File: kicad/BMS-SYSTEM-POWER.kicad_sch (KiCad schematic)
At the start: 80 parts, among them J1 BATTERY, J2 USB C, Q1 AO4435, Q11 2N3904, Q17 2N3904, Q2 AO4468, Q3 PNP-SOT23, Q4 WST4041, Q5 AO3401, U1 SGM6132YPS8G/TR, U2 CN3303, U4 SY8089A, U5 SY8089A, U6 INA180A2IDBVR

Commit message: Battery charging
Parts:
- removed C4, C7: 22uF, oomwoo_altium:C1206, symbol DesignLibrary:POWER_1_Capacitor-1_DesignLibrary.SchLib
- removed D1: SS34, oomwoo_altium:SMA, symbol DesignLibrary:POWER_0_DIODE-2_DesignLibrary.SchLib
- removed D3: SS54/NC, oomwoo_altium:SMB_L4.3-W3.6-LS5.4-RD, symbol DesignLibrary:POWER_2_DIODE-2_DesignLibrary.SchLib
- removed D4: SS34, oomwoo_altium:SMA, symbol DesignLibrary:POWER_1_DIODE-2_DesignLibrary.SchLib
- removed D5: SS54, oomwoo_altium:SMB_L4.3-W3.6-LS5.4-RD, symbol DesignLibrary:POWER_0_DIODE-2_DesignLibrary.SchLib
- removed J1: BATTERY, oomwoo_altium:CONN-SMD_4P-P2.00_XUNPU_WAFER-PH2.0-4PWB, symbol DesignLibrary:POWER_2_HDRx4_DesignLibrary.SchLib
- removed J2: USB C, oomwoo_altium:CONN-SMD_4P-P2.00_XUNPU_WAFER-PH2.0-4PWB, symbol DesignLibrary:POWER_0_HDRx4_DesignLibrary.SchLib
- removed L1: 6.8uH, oomwoo_altium:IND-SMD_L7.0-W6.6, symbol DesignLibrary:POWER_0_INDUCTOR-SMD_DesignLibrary.SchLib
- removed Q1: AO4435, oomwoo_altium:SOP-8_L4.9-W3.9-P1.27-LS6.0-BL-1, symbol DesignLibrary:POWER_1_mirrored_AO4407A_DesignLibrary.SchLib
- removed Q2: AO4468, oomwoo_altium:SOP-8_L4.9-W3.9-P1.27-LS6.0-BL-1, symbol DesignLibrary:POWER_0_NCE3018AS_DesignLibrary.SchLib
- removed Q4: WST4041, oomwoo_altium:SOT23-3D, symbol DesignLibrary:POWER_1_P-MOS-SOT23_DesignLibrary.SchLib
- removed R13: 100K, oomwoo_altium:RES-0402, symbol DesignLibrary:POWER_1_Resistor-1_DesignLibrary.SchLib
- removed R2: 40mR, oomwoo_altium:R1210, symbol DesignLibrary:POWER_0_Resistor-1_DesignLibrary.SchLib
- removed R3: 2K, oomwoo_altium:RES-0402, symbol DesignLibrary:POWER_2_Resistor-1_DesignLibrary.SchLib
- removed R5: 100K, oomwoo_altium:RES-0402, symbol DesignLibrary:POWER_2_Resistor-1_DesignLibrary.SchLib
- removed R6: 35K, oomwoo_altium:RES-0402, symbol DesignLibrary:POWER_2_Resistor-1_DesignLibrary.SchLib
- removed U2: CN3303, oomwoo_altium:SOP-8_L4.9-W3.9-P1.27-LS6.0-BL-1, symbol DesignLibrary:POWER_0_CN3303_DesignLibrary.SchLib
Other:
- note added: "CAN BE REMOVED"
- note added: "POWER MANAGMENT"
- note removed: "BATTERY CHARGE AND POWER MANAGMENT"
- moved on the sheet: C28, R30, R33, U6

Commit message: Added Pi CM4/CM5
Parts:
- removed C1, C14: 10nF, oomwoo_altium:CAP-0402, symbol DesignLibrary:POWER_2_Capacitor-1_DesignLibrary.SchLib
- removed C10, C11, C12: 22uF, oomwoo_altium:CAP-0805-S, symbol DesignLibrary:POWER_1_Capacitor-1_DesignLibrary.SchLib
- removed C13: 0.1uF, oomwoo_altium:CAP-0402, symbol DesignLibrary:POWER_3_Capacitor-1_DesignLibrary.SchLib
- removed C15: 4.7uF, oomwoo_altium:CAP-0603, symbol DesignLibrary:POWER_1_Capacitor-1_DesignLibrary.SchLib
- removed C2, C3: 10uF, oomwoo_altium:CAP-0805-S, symbol DesignLibrary:POWER_1_Capacitor-1_DesignLibrary.SchLib
- removed C28: 100nF, oomwoo_altium:CAP-0402, symbol DesignLibrary:POWER_1_Capacitor-1_DesignLibrary.SchLib
- removed D2: SS34, oomwoo_altium:SMA, symbol DesignLibrary:POWER_2_DIODE-2_DesignLibrary.SchLib
- removed L2: 4.7uH, oomwoo_altium:IND-SMD_L7.0-W6.6, symbol DesignLibrary:POWER_0_INDUCTOR-SMD_DesignLibrary.SchLib
- removed Q17: 2N3904, oomwoo_altium:SOT23-3D, symbol DesignLibrary:POWER_0_NPN-SOT23_DesignLibrary.SchLib
- removed Q5: AO3401, oomwoo_altium:SOT23-3D, symbol DesignLibrary:POWER_1_mirrored_P-MOS-SOT23_DesignLibrary.SchLib
- removed R1: 10mR, oomwoo_altium:RES-1206, symbol DesignLibrary:POWER_0_Resistor-1_DesignLibrary.SchLib
- removed R12, R9: 100K, oomwoo_altium:RES-0402, symbol DesignLibrary:POWER_1_Resistor-1_DesignLibrary.SchLib
- removed R15: 22K, oomwoo_altium:RES-0402, symbol DesignLibrary:POWER_0_Resistor-1_DesignLibrary.SchLib
- removed R16: 1K, oomwoo_altium:RES-0402, symbol DesignLibrary:POWER_0_Resistor-1_DesignLibrary.SchLib
- removed R30: 132.5K, oomwoo_altium:RES-0402, symbol DesignLibrary:POWER_0_Resistor-1_DesignLibrary.SchLib
- removed R33: 47K, oomwoo_altium:RES-0402, symbol DesignLibrary:POWER_1_Resistor-1_DesignLibrary.SchLib
- removed R4: 52.3K, oomwoo_altium:RES-0402, symbol DesignLibrary:POWER_0_Resistor-1_DesignLibrary.SchLib
- removed R7: 10K, oomwoo_altium:RES-0402, symbol DesignLibrary:POWER_1_Resistor-1_DesignLibrary.SchLib
- removed R8: 15K, oomwoo_altium:RES-0402, symbol DesignLibrary:POWER_2_Resistor-1_DesignLibrary.SchLib
- removed U1: SGM6132YPS8G/TR, oomwoo_altium:SOIC-8_L4.9-W3.9-P1.27-LS6.0-BL-EP3.4, symbol DesignLibrary:POWER_0_SGM6132YPS8G/TR_DesignLibrary.SchLib
- removed U6: INA180A2IDBVR, oomwoo_altium:SOT_23_5, symbol DesignLibrary:POWER_0_INA180A2IDBVR_DesignLibrary.SchLib
- added C36: 10uF/50V, JLCImport:CL21A106KBYQNNE, symbol JLCImport:CL21A106KBYQNNE
- added C38, C40: 100nF 50V, Capacitor_SMD:C_0603_1608Metric, symbol Library:C_0603
- added C42: 47pF/16V, Capacitor_SMD:C_0603_1608Metric, symbol Device:C_Small
- added C44, C46: 22uF/16V, Capacitor_SMD:C_0805_2012Metric, symbol Device:C_Small
- added L1: 6.8uH, JLCImport:IHLP2525CZER6R8M01, symbol JLCImport:IHLP2525CZER6R8M01
- added R42: 158k, Resistor_SMD:R_0603_1608Metric, symbol Device:R_US
- added R43: 30.1k, Resistor_SMD:R_0603_1608Metric, symbol Device:R_US
- added U8: AP63300WU-7, JLCImport:AP63300WU-7, symbol JLCImport:AP63300WU-7
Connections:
- net VCC-5V-SYS is gone; now on net VCC-5V-REG: C22.2, C27.2, D26.1 (A), R11.1, R23.1, U4.4 (IN), U5.4 (IN)
- net BAT-VCC: now also C36.1, C38.1, U8.3 (VIN)
- net GND: now also C36.2, C38.2, C44.2, C46.2, R43.1, U8.4 (GND)
- net POWER-EN: now also U8.2 (EN)
- net VCC-5V-REG: now also C42.1, C44.1, C46.1, L1.2, R42.2
- new net: C42.2, R42.1, R43.2, U8.1 (FB)
- new net: C40.1, U8.6 (BST)
- new net SW_3.3: C40.2, L1.1, U8.5 (SW)
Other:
- note removed: "3A"
- note removed: "CAN BE REMOVED"
- note removed: "Default 5V"
- note removed: "VIN: 4.5V ~ 28.5V"
- moved on the sheet: D16, D23, D24, D25, D26, D27, D28, Q11, Q3, R10, R14, R28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

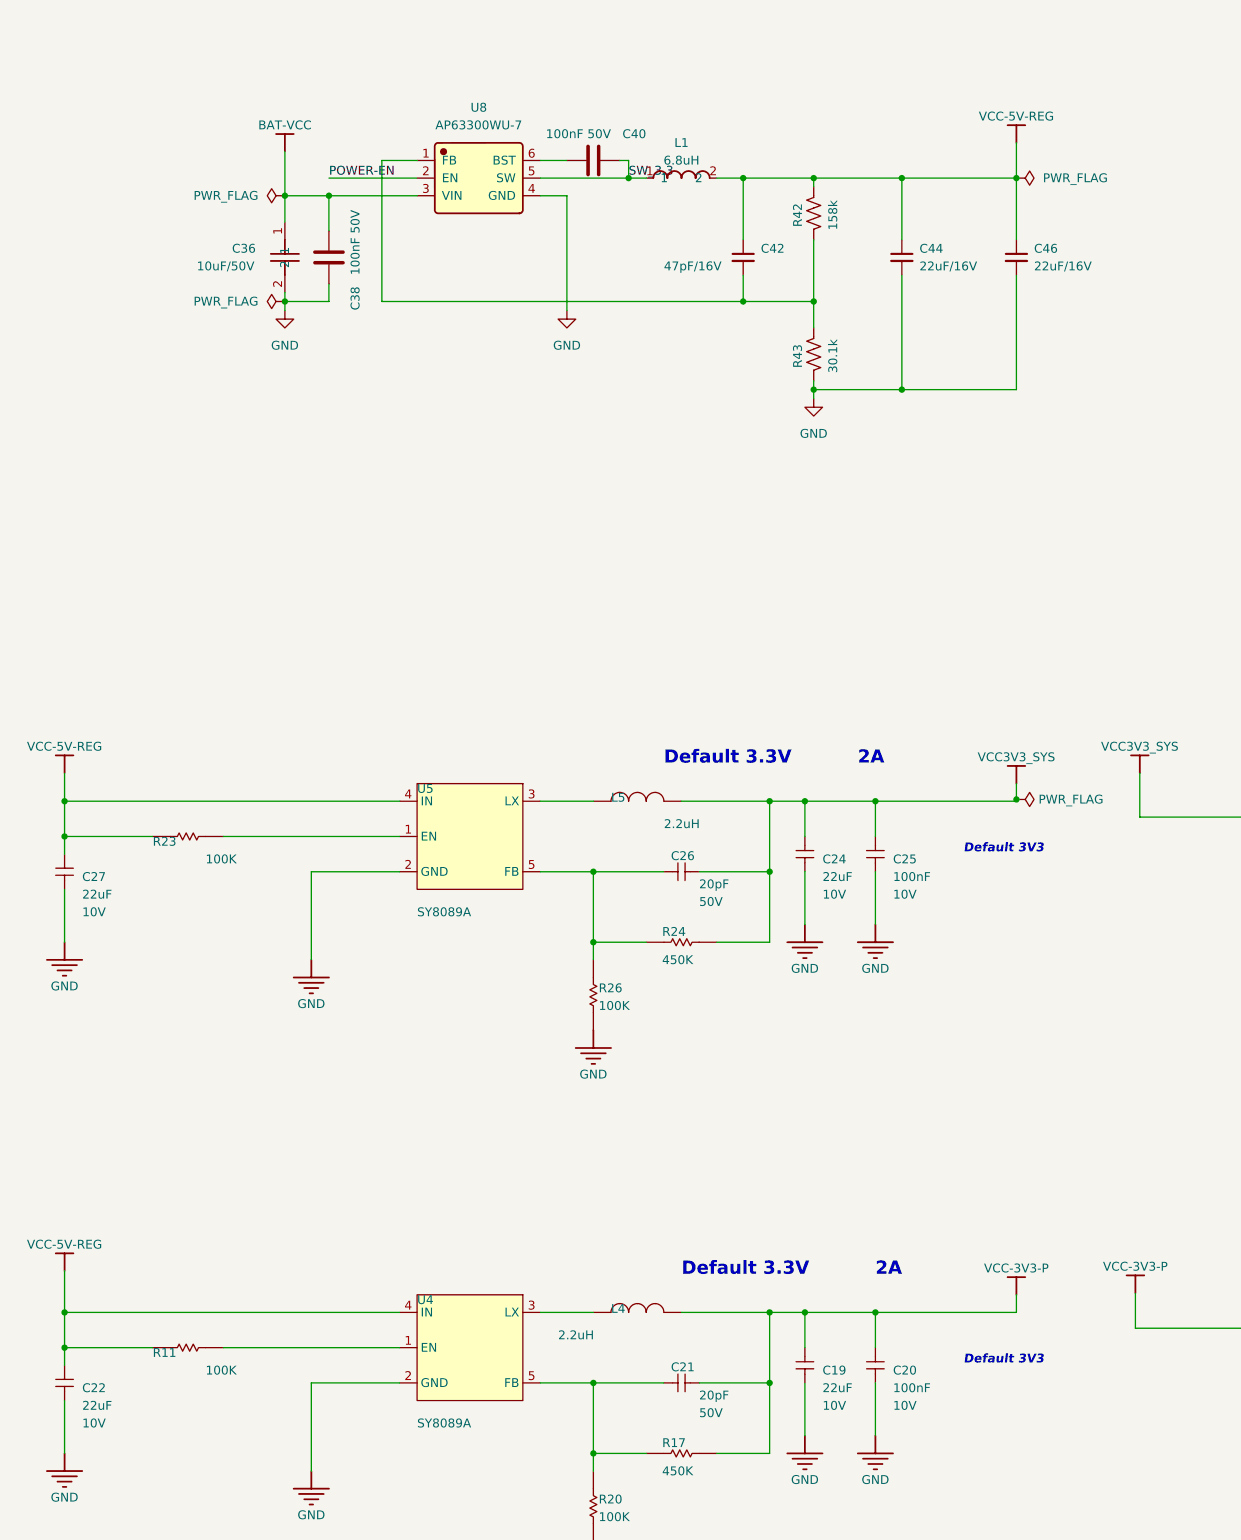
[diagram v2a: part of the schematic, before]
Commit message: Changed MCU to STM32G473VCT6
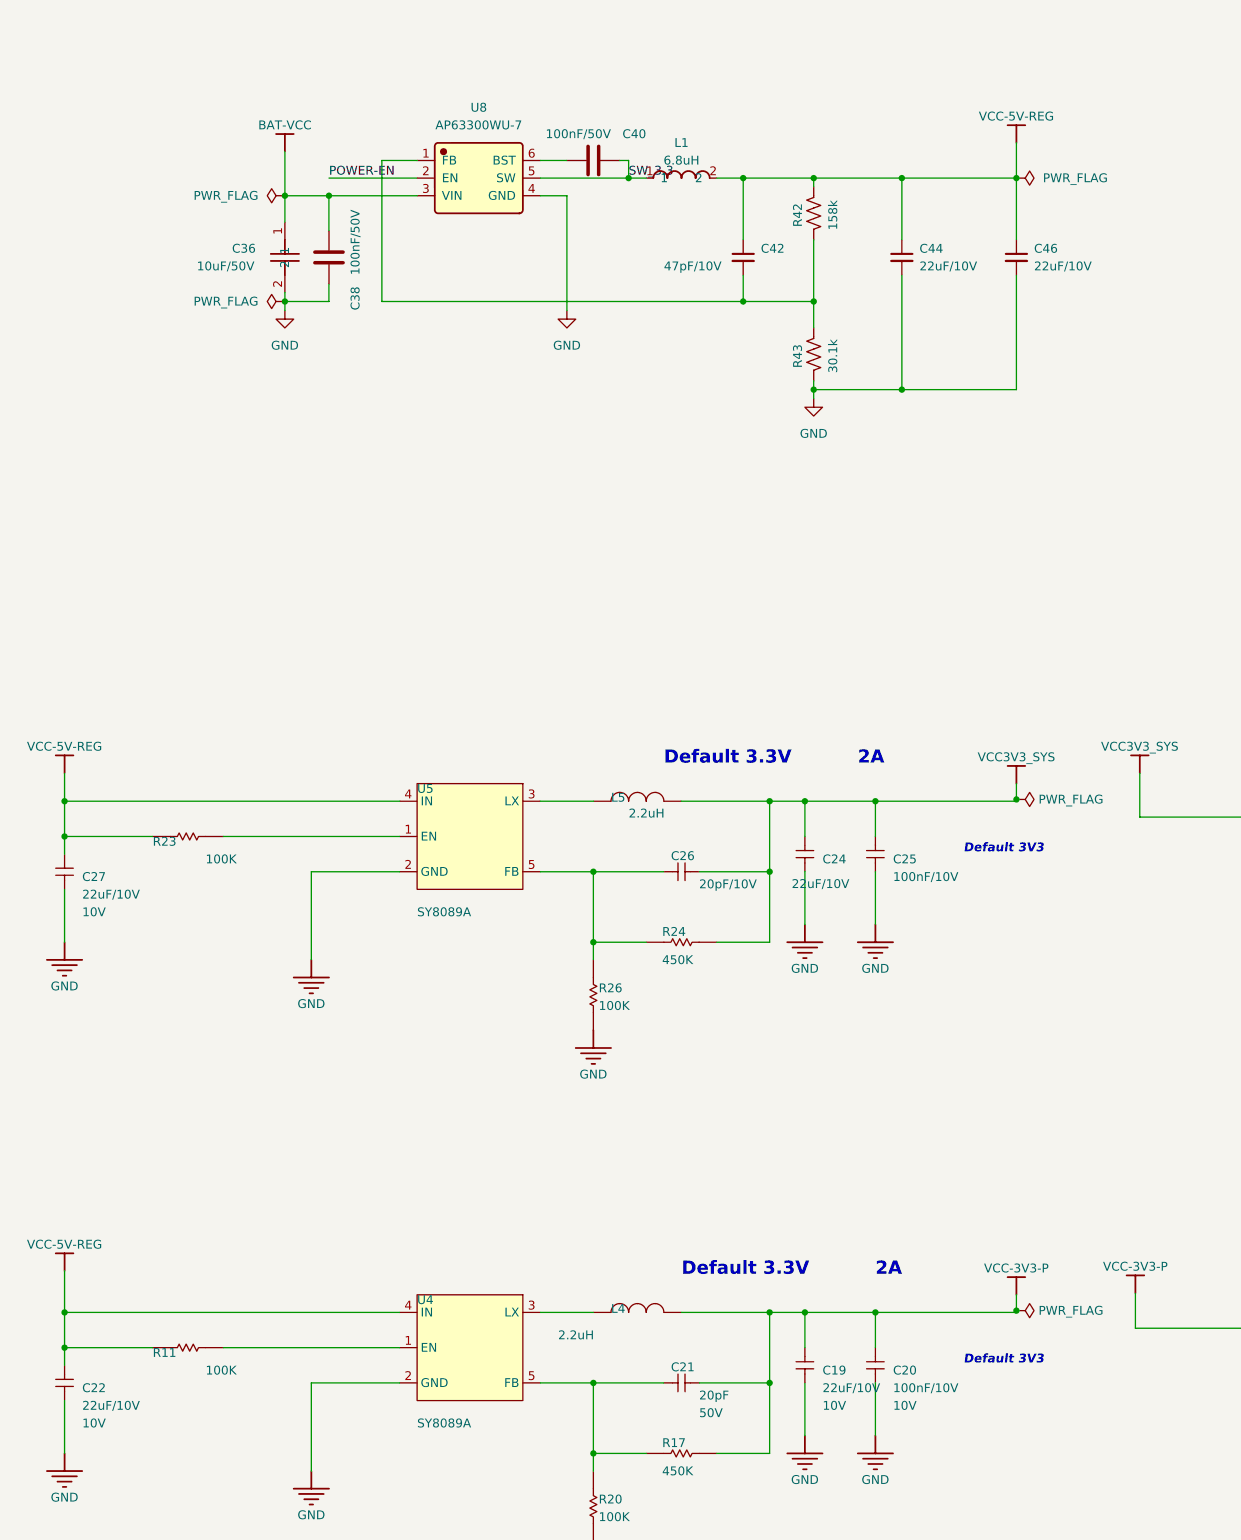
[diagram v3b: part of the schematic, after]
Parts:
- C19, C22, C24, C27: value 22uF -> 22uF/10V; footprint oomwoo_altium:CAP-0603 -> Capacitor_SMD:C_0603_1608Metric
- C20, C25: value 100nF -> 100nF/10V; footprint oomwoo_altium:CAP-0402 -> Capacitor_SMD:C_0603_1608Metric
- C21: footprint oomwoo_altium:CAP-0402 -> Capacitor_SMD:C_0603_1608Metric
- C26: value 20pF -> 20pF/10V; footprint oomwoo_altium:CAP-0402 -> Capacitor_SMD:C_0603_1608Metric
- C36: footprint JLCImport:CL21A106KBYQNNE -> Capacitor_SMD:C_0603_1608Metric
- C38, C40: value 100nF 50V -> 100nF/50V
- C42: value 47pF/16V -> 47pF/10V
- C44, C46: value 22uF/16V -> 22uF/10V
- R10, R11, R14, R17, R20, R23, R24, R26, R28, R29, R31, R32, R34, R40, R45: footprint oomwoo_altium:RES-0402 -> Resistor_SMD:R_0603_1608Metric
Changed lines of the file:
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@@
 	)
 	(junction
+		(at 187.96 257.175)
+		(diameter 0)
+		(color 0 0 0 0)
+	)
+	(junction
 		(at 171.45 93.98)
 		(diameter 0)
@@
 	(wire
 		(pts
+			(xy 187.96 257.175) (xy 187.96 257.429)
+		)
+		(stroke
+			(width 0)
+			(type default)
+		)
+	)
+	(wire
+		(pts
 			(xy 88.9 93.98) (xy 101.6 93.98)
 		)
@@
 	(wire
 		(pts
-			(xy 187.96 254.889) (xy 187.96 257.429)
+			(xy 187.96 254.889) (xy 187.96 257.175)
 		)
 		(stroke
@@
 			)
 		)
-		(property "Footprint" "oomwoo_altium:RES-0402"
+		(property "Footprint" "Resistor_SMD:R_0603_1608Metric"
 			(at 144.78 277.749 0)
 			(hide yes)
@@
 			)
 		)
-		(property "Footprint" "oomwoo_altium:RES-0402"
+		(property "Footprint" "Resistor_SMD:R_0603_1608Metric"
 			(at 400.685 186.69 0)
 			(hide yes)
@@
 			)
 		)
-		(property "Footprint" "oomwoo_altium:RES-0402"
+		(property "Footprint" "Resistor_SMD:R_0603_1608Metric"
 			(at 382.905 217.17 0)
 			(hide yes)
@@
 			)
 		)
-		(property "Footprint" "oomwoo_altium:RES-0402"
+		(property "Footprint" "Resistor_SMD:R_0603_1608Metric"
 			(at 451.485 186.69 0)
 			(hide yes)
@@
 			)
 		)
-		(property "Footprint" "oomwoo_altium:RES-0402"
+		(property "Footprint" "Resistor_SMD:R_0603_1608Metric"
 			(at 246.38 186.055 0)
 			(hide yes)
@@
 			)
 		)
-		(property "Footprint" "oomwoo_altium:RES-0402"
+		(property "Footprint" "Resistor_SMD:R_0603_1608Metric"
 			(at 245.745 259.715 0)
 			(hide yes)
@@
 		)
 		(property "Value" "2.2uH"
-			(at 137.16 186.309 90)
+			(at 132.08 184.785 90)
 			(show_name no)
 			(do_not_autoplace no)
@@
 			)
 		)
-		(property "Footprint" "oomwoo_altium:RES-0402"
+		(property "Footprint" "Resistor_SMD:R_0603_1608Metric"
 			(at 144.78 204.089 0)
 			(hide yes)
@@
 			)
 		)
-		(property "Value" "22uF"
-			(at 160.02 193.929 0)
+		(property "Value" "22uF/10V"
+			(at 155.575 194.945 0)
 			(show_name no)
 			(do_not_autoplace no)
@@
 			)
 		)
-		(property "Footprint" "oomwoo_altium:CAP-0603"
+		(property "Footprint" "Capacitor_SMD:C_0603_1608Metric"
 			(at 157.48 193.929 0)
 			(hide yes)
@@
 		(property "VOLTAGERATE" "10V"
 			(at 160.02 196.469 0)
+			(hide yes)
 			(show_name no)
 			(do_not_autoplace no)
@@
 			)
 		)
-		(property "Footprint" "oomwoo_altium:RES-0402"
+		(property "Footprint" "Resistor_SMD:R_0603_1608Metric"
 			(at 367.665 201.93 0)
 			(hide yes)
@@
 			)
 		)
-		(property "Value" "22uF"
+		(property "Value" "22uF/10V"
 			(at 53.34 196.469 0)
 			(show_name no)
@@
 			)
 		)
-		(property "Footprint" "oomwoo_altium:CAP-0603"
+		(property "Footprint" "Capacitor_SMD:C_0603_1608Metric"
 			(at 50.8 196.469 0)
 			(hide yes)
@@
 			)
 		)
-		(property "Footprint" "oomwoo_altium:RES-0402"
+		(property "Footprint" "Resistor_SMD:R_0603_1608Metric"
 			(at 127 280.289 0)
 			(hide yes)
@@
 			)
 		)
-		(property "Value" "22uF/16V"
+		(property "Value" "22uF/10V"
 			(at 173.99 106.6862 0)
 			(show_name no)
@@
 			)
 		)
-		(property "Footprint" "oomwoo_altium:RES-0402"
+		(property "Footprint" "Resistor_SMD:R_0603_1608Metric"
 			(at 451.485 171.45 0)
 			(hide yes)
@@
 			)
 		)
-		(property "Value" "22uF"
+		(property "Value" "22uF/10V"
 			(at 160.02 267.589 0)
 			(show_name no)
@@
 			)
 		)
-		(property "Footprint" "oomwoo_altium:CAP-0603"
+		(property "Footprint" "Capacitor_SMD:C_0603_1608Metric"
 			(at 157.48 267.589 0)
 			(hide yes)
@@
 			)
 		)
-		(property "Footprint" "oomwoo_altium:RES-0402"
+		(property "Footprint" "Resistor_SMD:R_0603_1608Metric"
 			(at 63.5 188.849 0)
 			(hide yes)
@@
 			)
 		)
-		(property "Value" "47pF/16V"
+		(property "Value" "47pF/10V"
 			(at 137.16 106.68 0)
 			(show_name no)
@@
 			)
 		)
-		(property "Value" "100nF"
+		(property "Value" "100nF/10V"
 			(at 170.18 193.929 0)
 			(show_name no)
@@
 			)
 		)
-		(property "Footprint" "oomwoo_altium:CAP-0402"
+		(property "Footprint" "Capacitor_SMD:C_0603_1608Metric"
 			(at 167.64 193.929 0)
 			(hide yes)
@@
 		(property "VOLTAGERATE" "10V"
 			(at 170.18 196.469 0)
+			(hide yes)
 			(show_name no)
 			(do_not_autoplace no)
@@
 			)
 		)
-		(property "Footprint" "oomwoo_altium:CAP-0402"
+		(property "Footprint" "Capacitor_SMD:C_0603_1608Metric"
 			(at 142.24 267.589 0)
 			(hide yes)
@@
 			)
 		)
-		(property "Footprint" "JLCImport:CL21A106KBYQNNE"
+		(property "Footprint" "Capacitor_SMD:C_0603_1608Metric"
 			(at 82.55 105.41 0)
 			(hide yes)
@@
 			)
 		)
-		(property "Footprint" "oomwoo_altium:RES-0402"
+		(property "Footprint" "Resistor_SMD:R_0603_1608Metric"
 			(at 446.405 196.85 0)
 			(hide yes)
@@
 			)
 		)
-		(property "Value" "100nF"
+		(property "Value" "100nF/10V"
 			(at 170.18 267.589 0)
 			(show_name no)
@@
 			)
 		)
-		(property "Footprint" "oomwoo_altium:CAP-0402"
+		(property "Footprint" "Capacitor_SMD:C_0603_1608Metric"
 			(at 167.64 267.589 0)
 			(hide yes)
@@
 			)
 		)
-		(property "Value" "22uF/16V"
+		(property "Value" "22uF/10V"
 			(at 190.5 106.6862 0)
 			(show_name no)
@@
 	)
 	(symbol
+		(lib_id "power:PWR_FLAG")
+		(at 187.96 257.175 270)
+		(unit 1)
+		(body_style 1)
+		(exclude_from_sim no)
+		(in_bom yes)
+		(on_board yes)
+		(in_pos_files yes)
+		(dnp no)
+		(fields_autoplaced yes)
+		(property "Reference" "#FLG016"
+			(at 189.865 257.175 0)
+			(hide yes)
+			(show_name no)
+			(do_not_autoplace no)
+			(effects
+				(font
+					(size 1.27 1.27)
+				)
+			)
+		)
+		(property "Value" "PWR_FLAG"
+			(at 191.135 257.1749 90)
+			(show_name no)
+			(do_not_autoplace no)
+			(effects
+				(font
+					(size 1.27 1.27)
+				)
+				(justify left)
+			)
+		)
+		(property "Footprint" ""
+			(at 187.96 257.175 0)
+			(hide yes)
+			(show_name no)
+			(do_not_autoplace no)
+			(effects
+				(font
+					(size 1.27 1.27)
+				)
+			)
+		)
+		(property "Datasheet" ""
+			(at 187.96 257.175 0)
+			(hide yes)
+			(show_name no)
+			(do_not_autoplace no)
+			(effects
+				(font
+					(size 1.27 1.27)
+				)
+			)
+		)
+		(property "Description" "Special symbol for telling ERC where power comes from"
+			(at 187.96 257.175 0)
+			(hide yes)
+			(show_name no)
+			(do_not_autoplace no)
+			(effects
+				(font
+					(size 1.27 1.27)
+				)
+			)
+		)
+		(pin "1"
+		)
+		(instances
+			(project "oomwoo-kicad"
+				(path "/dbcfb655-8d45-4808-9a74-2a0eb03372e8/35c833ed-33c3-4a72-8fc9-e035e67a6b75"
+					(reference "#FLG016")
+					(unit 1)
+				)
+			)
+		)
+	)
+	(symbol
 		(lib_id "JLCImport:AP63300WU-7")
 		(at 110.49 93.98 0)
@@
 			)
 		)
-		(property "Value" "100nF 50V"
+		(property "Value" "100nF/50V"
 			(at 92.71 107.95 90)
 			(show_name no)
@@
 			)
 		)
-		(property "Value" "20pF"
+		(property "Value" "20pF/10V"
 			(at 142.24 196.469 90)
 			(show_name no)
@@
 			)
 		)
-		(property "Footprint" "oomwoo_altium:CAP-0402"
+		(property "Footprint" "Capacitor_SMD:C_0603_1608Metric"
 			(at 142.24 193.929 0)
 			(hide yes)
@@
 		(property "VOLTAGERATE" "50V"
 			(at 142.24 199.009 90)
+			(hide yes)
 			(show_name no)
 			(do_not_autoplace no)
@@
 			)
 		)
-		(property "Footprint" "oomwoo_altium:RES-0402"
+		(property "Footprint" "Resistor_SMD:R_0603_1608Metric"
 			(at 63.5 262.509 0)
 			(hide yes)
@@
 			)
 		)
-		(property "Value" "22uF"
+		(property "Value" "22uF/10V"
 			(at 53.34 270.129 0)
 			(show_name no)
@@
 			)
 		)
-		(property "Footprint" "oomwoo_altium:CAP-0603"
+		(property "Footprint" "Capacitor_SMD:C_0603_1608Metric"
 			(at 50.8 270.129 0)
 			(hide yes)
@@
 			)
 		)
-		(property "Value" "100nF 50V"
+		(property "Value" "100nF/50V"
 			(at 129.54 87.63 90)
 			(show_name no)
@@
 			)
 		)
-		(property "Footprint" "oomwoo_altium:RES-0402"
+		(property "Footprint" "Resistor_SMD:R_0603_1608Metric"
 			(at 441.325 204.47 0)
 			(hide yes)
@@
 			)
 		)
-		(property "Footprint" "oomwoo_altium:RES-0402"
+		(property "Footprint" "Resistor_SMD:R_0603_1608Metric"
 			(at 127 206.629 0)
 			(hide yes)

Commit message: STM32G473VCT6
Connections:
- net VCC3V3_SYS renamed VCC3V3_M2
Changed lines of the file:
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@@
 			)
 		)
-		(property "Value" "VCC3V3_SYS"
+		(property "Value" "VCC3V3_M2"
 			(at 205.74 175.895 0)
 			(show_name no)
@@
 			)
 		)
-		(property "Value" "VCC3V3_SYS"
+		(property "Value" "VCC3V3_M2"
 			(at 187.96 177.419 0)
 			(show_name no)
